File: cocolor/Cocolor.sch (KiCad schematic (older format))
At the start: 17 parts, among them P1 CONN_01X05, P2 CONN_01X05, U1 TCS3472, U2 LTC4316

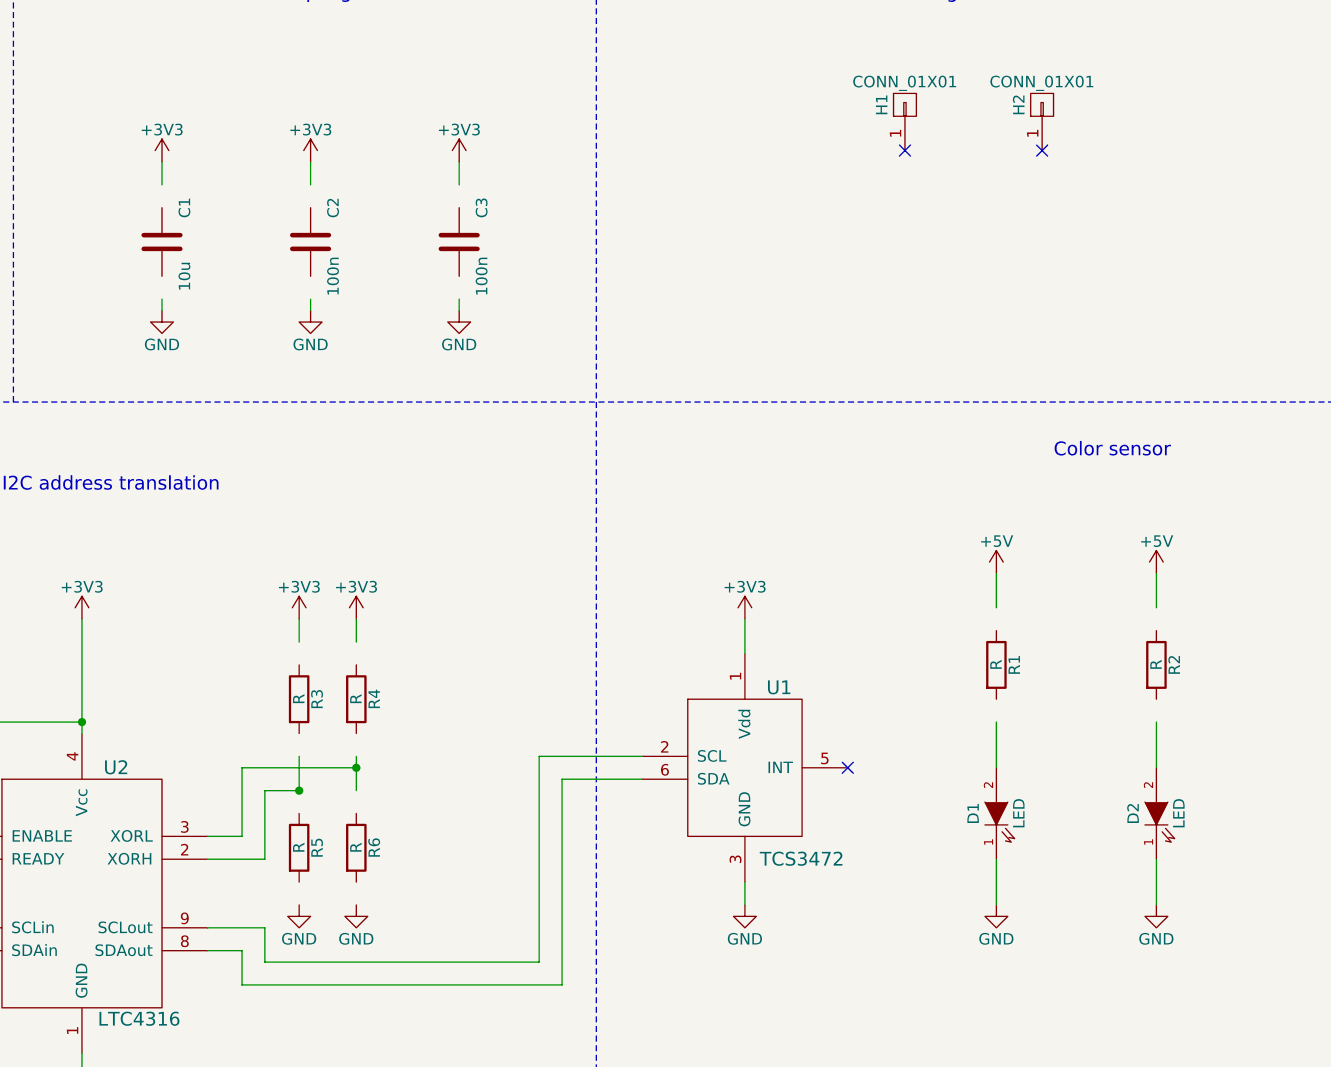
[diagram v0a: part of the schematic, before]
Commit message: fix schematic of cocolor board
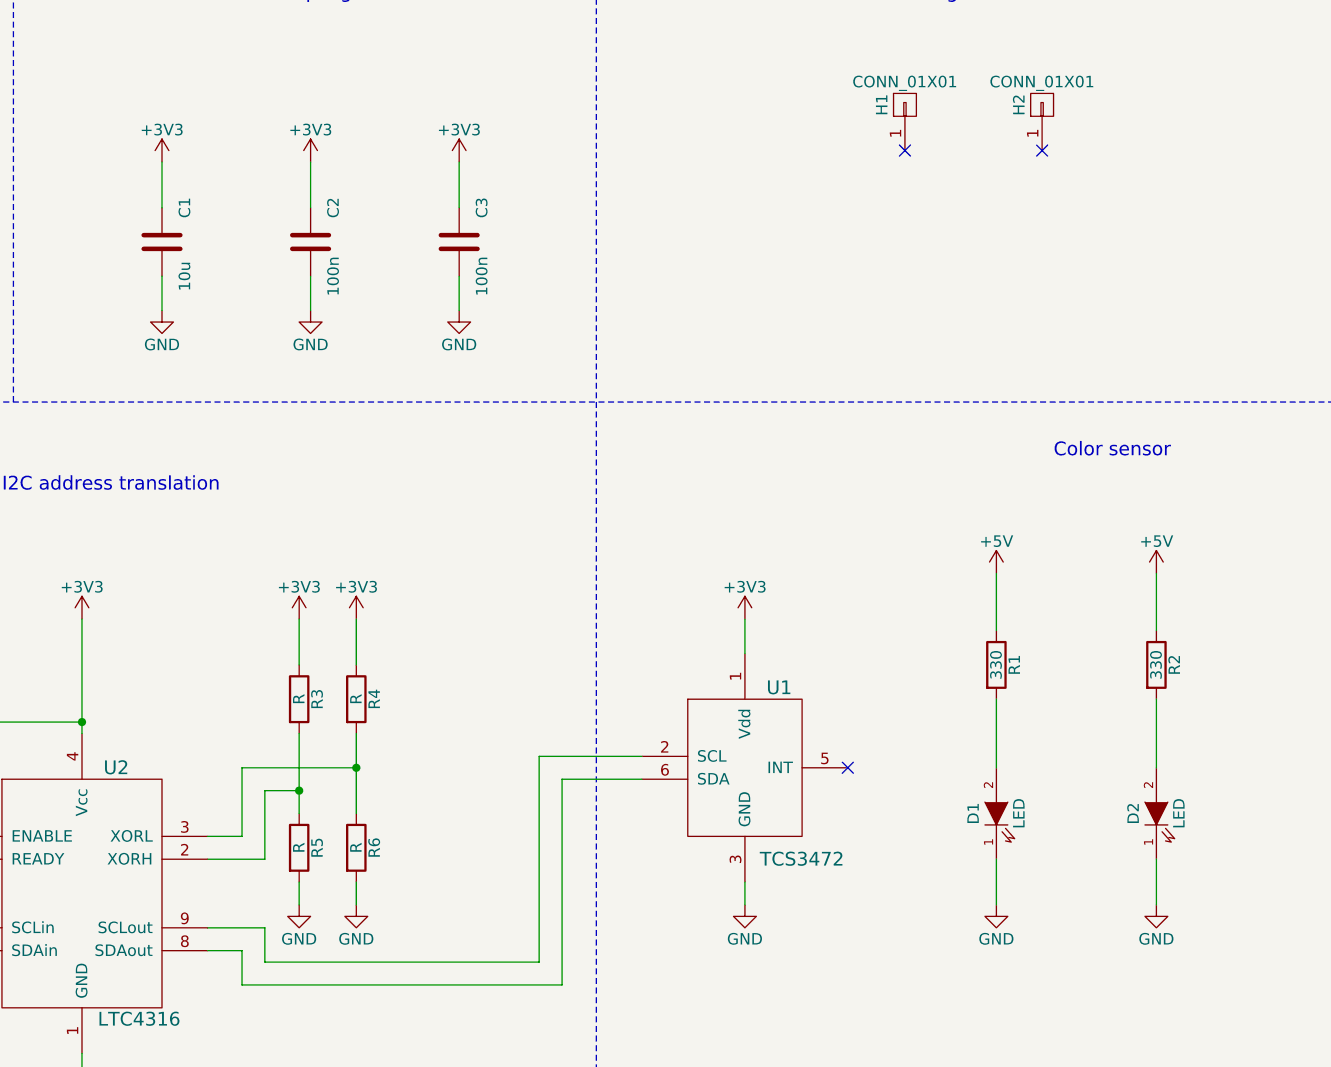
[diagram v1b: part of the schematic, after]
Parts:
- R1, R2: value R -> 330
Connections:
- wire segments 57 -> 59
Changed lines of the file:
@@
 LIBS:regul
 LIBS:references
-LIBS:pspice
 LIBS:powerint
 LIBS:power
@@
 	3400 2600 3400 500
 $Comp
-L C C1
-U 1 1 573CB74D
-P 4050 1900
-F 0 "C1" V 4150 2050 50  0000 C CNN
-F 1 "10u" V 4150 1750 50  0000 C CNN
-F 2 "" H 4050 1900 50  0000 C CNN
-F 3 "" H 4050 1900 50  0000 C CNN
-	1    4050 1900
-	1    0    0    -1
-$EndComp
-$Comp
 L GND #PWR05
 U 1 1 573CB77A
@@
 $EndComp
 $Comp
-L C C2
-U 1 1 573CB7A2
-P 4700 1900
-F 0 "C2" V 4800 2050 50  0000 C CNN
-F 1 "100n" V 4800 1750 50  0000 C CNN
-F 2 "" H 4700 1900 50  0000 C CNN
-F 3 "" H 4700 1900 50  0000 C CNN
-	1    4700 1900
-	1    0    0    -1
-$EndComp
-$Comp
 L GND #PWR07
 U 1 1 573CB7D4
@@
 $EndComp
 Wire Wire Line
-	4050 1550 4050 1650
-Wire Wire Line
-	4050 2150 4050 2200
-Wire Wire Line
-	4700 1550 4700 1650
-Wire Wire Line
-	4700 2150 4700 2200
+	4050 1550 4050 1750
+Wire Wire Line
+	4050 2050 4050 2200
+Wire Wire Line
+	4700 1550 4700 1750
+Wire Wire Line
+	4700 2050 4700 2200
 Text Notes 4150 850  0    60   ~ 0
 Power decoupling
@@
 	4400 4200 4900 4200
 Wire Wire Line
-	4900 4150 4900 4300
-Wire Wire Line
-	4650 4300 4650 4150
+	4900 4050 4900 4400
+Wire Wire Line
+	4650 4050 4650 4400
 Connection ~ 4900 4200
 Connection ~ 4650 4300
@@
 $EndComp
 Wire Wire Line
-	4900 3550 4900 3650
-Wire Wire Line
-	4650 3650 4650 3550
+	4900 3550 4900 3750
+Wire Wire Line
+	4650 3550 4650 3750
 $Comp
 L GND #PWR015
@@
 $EndComp
 $Comp
-L C C3
-U 1 1 573CD222
-P 5350 1900
-F 0 "C3" V 5450 2050 50  0000 C CNN
-F 1 "100n" V 5450 1750 50  0000 C CNN
-F 2 "" H 5350 1900 50  0000 C CNN
-F 3 "" H 5350 1900 50  0000 C CNN
-	1    5350 1900
-	1    0    0    -1
-$EndComp
-$Comp
 L +3V3 #PWR016
 U 1 1 573CD3DF
@@
 $EndComp
 Wire Wire Line
-	5350 1550 5350 1650
-Wire Wire Line
-	5350 2200 5350 2150
+	5350 1550 5350 1750
+Wire Wire Line
+	5350 2050 5350 2200
 $Comp
 L TCS3472 U1
@@
 P 8400 3750
 F 0 "R2" V 8480 3750 50  0000 C CNN
-F 1 "R" V 8400 3750 50  0000 C CNN
+F 1 "330" V 8400 3750 50  0000 C CNN
 F 2 "" H 8400 3750 50  0000 C CNN
 F 3 "" H 8400 3750 50  0000 C CNN
@@
 $EndComp
 Wire Wire Line
-	8400 4200 8400 4000
-Wire Wire Line
-	8400 3500 8400 3350
+	8400 3900 8400 4200
+Wire Wire Line
+	8400 3350 8400 3600
 $Comp
 L LED D1
@@
 P 7700 3750
 F 0 "R1" V 7780 3750 50  0000 C CNN
-F 1 "R" V 7700 3750 50  0000 C CNN
+F 1 "330" V 7700 3750 50  0000 C CNN
 F 2 "" H 7700 3750 50  0000 C CNN
 F 3 "" H 7700 3750 50  0000 C CNN
@@
 $EndComp
 Wire Wire Line
-	7700 4200 7700 4000
-Wire Wire Line
-	7700 3500 7700 3350
+	7700 3900 7700 4200
+Wire Wire Line
+	7700 3350 7700 3600
 $Comp
 L CONN_01X01 H1
@@
 NoConn ~ 7300 1500
 NoConn ~ 7900 1500
+$Comp
+L C C3
+U 1 1 573CD222
+P 5350 1900
+F 0 "C3" V 5450 2050 50  0000 C CNN
+F 1 "100n" V 5450 1750 50  0000 C CNN
+F 2 "" H 5350 1900 50  0000 C CNN
+F 3 "" H 5350 1900 50  0000 C CNN
+	1    5350 1900
+	1    0    0    -1
+$EndComp
+$Comp
+L C C2
+U 1 1 573CB7A2
+P 4700 1900
+F 0 "C2" V 4800 2050 50  0000 C CNN
+F 1 "100n" V 4800 1750 50  0000 C CNN
+F 2 "" H 4700 1900 50  0000 C CNN
+F 3 "" H 4700 1900 50  0000 C CNN
+	1    4700 1900
+	1    0    0    -1
+$EndComp
+$Comp
+L C C1
+U 1 1 573CB74D
+P 4050 1900
+F 0 "C1" V 4150 2050 50  0000 C CNN
+F 1 "10u" V 4150 1750 50  0000 C CNN
+F 2 "" H 4050 1900 50  0000 C CNN
+F 3 "" H 4050 1900 50  0000 C CNN
+	1    4050 1900
+	1    0    0    -1
+$EndComp
+Wire Wire Line
+	4650 4700 4650 4800
+Wire Wire Line
+	4900 4800 4900 4700
 $EndSCHEMATC

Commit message: cocolor layout
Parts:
- C1: footprint (none) -> espitall:C_0805_HandSoldering
- C2, C3: footprint (none) -> espitall:C_0603_HandSoldering
- D1, D2: footprint (none) -> espitall:LED_1206
- H1, H2: footprint (none) -> Mounting_Holes:MountingHole_3.2mm_M3
- P1, P2: footprint (none) -> espitall:Socket_MOLEX-KK-RM2-54mm_Lock_5pin_straight
- R1, R2, R3, R4, R5, R6: footprint (none) -> espitall:R_0603_HandSoldering
- U1: footprint (none) -> espitall:DFN-6
- U2: footprint (none) -> espitall:MSOP-10
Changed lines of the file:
@@
-EESchema Schematic File Version 2
-LIBS:xilinx
-LIBS:video
-LIBS:valves
-LIBS:ttl_ieee
-LIBS:transistors
-LIBS:transf
-LIBS:texas
-LIBS:switches
-LIBS:supertex
-LIBS:stm8
-LIBS:stm32
-LIBS:siliconi
-LIBS:silabs
-LIBS:sensors
-LIBS:rfcom
-LIBS:relays
-LIBS:regul
-LIBS:references
-LIBS:powerint
-LIBS:power
-LIBS:philips
-LIBS:opto
-LIBS:onsemi
-LIBS:nxp_armmcu
-LIBS:nordicsemi
-LIBS:msp430
-LIBS:motorola
-LIBS:motor_drivers
-LIBS:microcontrollers
-LIBS:microchip_pic32mcu
-LIBS:microchip_pic18mcu
-LIBS:microchip_pic16mcu
-LIBS:microchip_pic12mcu
-LIBS:microchip_pic10mcu
-LIBS:microchip_dspic33dsc
-LIBS:microchip
-LIBS:memory
-LIBS:maxim
-LIBS:logo
-LIBS:linear
-LIBS:ir
-LIBS:interface
-LIBS:intel
-LIBS:hc11
-LIBS:graphic
-LIBS:gennum
-LIBS:ftdi
-LIBS:elec-unifil
-LIBS:dsp
-LIBS:display
-LIBS:diode
-LIBS:digital-audio
-LIBS:device
-LIBS:dc-dc
-LIBS:cypress
-LIBS:contrib
-LIBS:conn
-LIBS:cmos_ieee
-LIBS:cmos4000
-LIBS:brooktre
-LIBS:audio
-LIBS:atmel
-LIBS:analog_switches
-LIBS:analog_devices
-LIBS:adc-dac
-LIBS:actel
-LIBS:ac-dc
-LIBS:Zilog
-LIBS:Xicor
-LIBS:Power_Management
-LIBS:Oscillators
-LIBS:Lattice
-LIBS:ESD_Protection
-LIBS:Altera
-LIBS:74xx
-LIBS:74xgxx
-LIBS:Symbols_Transformer-Diskrete_RevA
-LIBS:Symbols_Socket-DIN41612_RevA
-LIBS:Symbols_Microcontroller_Philips-NXP_RevA_06Oct2013
-LIBS:Symbols_ICs-Opto_RevB_16Sep2013
-LIBS:Symbols_ICs-Diskrete_RevD10
-LIBS:Symbols_EN60617_13Mar2013
-LIBS:Symbols_EN60617-10_HF-Radio_DRAFT_12Sep2013
-LIBS:Symbols_DCDC-ACDC-Converter_RevC_20Jul2012
-LIBS:SymbolsSimilarEN60617+oldDIN617-RevE8
+EESchema Schematic File Version 3
 LIBS:espitall
 LIBS:Cocolor-cache
-EELAYER 25 0
+EELAYER 26 0
 EELAYER END
 $Descr A4 11693 8268
@@
 	2100 5000 2100 1900
 Connection ~ 2100 1900
-$Comp
-L LTC4316 U2
-U 1 1 573CCB68
-P 3700 4750
-F 0 "U2" H 3850 5300 60  0000 C CNN
-F 1 "LTC4316" H 3950 4200 60  0000 C CNN
-F 2 "" H 3700 4750 60  0000 C CNN
-F 3 "" H 3700 4750 60  0000 C CNN
-	1    3700 4750
-	1    0    0    -1
-$EndComp
 Wire Wire Line
 	3150 4500 3050 4500
@@
 F 0 "R3" V 4730 3900 50  0000 C CNN
 F 1 "R" V 4650 3900 50  0000 C CNN
-F 2 "" H 4650 3900 50  0000 C CNN
+F 2 "espitall:R_0603_HandSoldering" H 4650 3900 50  0001 C CNN
 F 3 "" H 4650 3900 50  0000 C CNN
 	1    4650 3900
-	1    0    0    -1
-$EndComp
-$Comp
-L R R5
-U 1 1 573CCC89
-P 4650 4550
-F 0 "R5" V 4730 4550 50  0000 C CNN
-F 1 "R" V 4650 4550 50  0000 C CNN
-F 2 "" H 4650 4550 50  0000 C CNN
-F 3 "" H 4650 4550 50  0000 C CNN
-	1    4650 4550
-	1    0    0    -1
-$EndComp
-$Comp
-L R R6
-U 1 1 573CCCC4
-P 4900 4550
-F 0 "R6" V 4980 4550 50  0000 C CNN
-F 1 "R" V 4900 4550 50  0000 C CNN
-F 2 "" H 4900 4550 50  0000 C CNN
-F 3 "" H 4900 4550 50  0000 C CNN
-	1    4900 4550
-	1    0    0    -1
-$EndComp
-$Comp
-L R R4
-U 1 1 573CCCF6
-P 4900 3900
-F 0 "R4" V 4980 3900 50  0000 C CNN
-F 1 "R" V 4900 3900 50  0000 C CNN
-F 2 "" H 4900 3900 50  0000 C CNN
-F 3 "" H 4900 3900 50  0000 C CNN
-	1    4900 3900
 	1    0    0    -1
 $EndComp
@@
 	5350 2050 5350 2200
 $Comp
-L TCS3472 U1
-U 1 1 573CD6D5
-P 6600 4200
-F 0 "U1" H 6750 4550 60  0000 C CNN
-F 1 "TCS3472" H 6850 3800 60  0000 C CNN
-F 2 "" H 6600 4200 60  0000 C CNN
-F 3 "" H 6600 4200 60  0000 C CNN
-	1    6600 4200
-	1    0    0    -1
-$EndComp
-$Comp
 L +3V3 #PWR017
 U 1 1 573CD7A4
@@
 F 0 "P1" H 1250 2200 50  0000 C CNN
 F 1 "CONN_01X05" V 1350 1900 50  0000 C CNN
-F 2 "" H 1250 1900 50  0000 C CNN
+F 2 "espitall:Socket_MOLEX-KK-RM2-54mm_Lock_5pin_straight" H 1250 1900 50  0001 C CNN
 F 3 "" H 1250 1900 50  0000 C CNN
 	1    1250 1900
@@
 F 0 "P2" H 2750 2200 50  0000 C CNN
 F 1 "CONN_01X05" V 2850 1900 50  0000 C CNN
-F 2 "" H 2750 1900 50  0000 C CNN
+F 2 "espitall:Socket_MOLEX-KK-RM2-54mm_Lock_5pin_straight" H 2750 1900 50  0001 C CNN
 F 3 "" H 2750 1900 50  0000 C CNN
 	1    2750 1900
@@
 Wire Wire Line
 	2500 1700 2550 1700
-$Comp
-L LED D2
-U 1 1 573CE5E1
-P 8400 4400
-F 0 "D2" H 8400 4500 50  0000 C CNN
-F 1 "LED" H 8400 4300 50  0000 C CNN
-F 2 "" H 8400 4400 50  0000 C CNN
-F 3 "" H 8400 4400 50  0000 C CNN
-	1    8400 4400
-	0    -1   -1   0
-$EndComp
 $Comp
 L GND #PWR021
@@
 	1    0    0    -1
 $EndComp
-$Comp
-L R R2
-U 1 1 573CE7BD
-P 8400 3750
-F 0 "R2" V 8480 3750 50  0000 C CNN
-F 1 "330" V 8400 3750 50  0000 C CNN
-F 2 "" H 8400 3750 50  0000 C CNN
-F 3 "" H 8400 3750 50  0000 C CNN
-	1    8400 3750
-	1    0    0    -1
-$EndComp
 Wire Wire Line
 	8400 3900 8400 4200
@@
 F 0 "D1" H 7700 4500 50  0000 C CNN
 F 1 "LED" H 7700 4300 50  0000 C CNN
-F 2 "" H 7700 4400 50  0000 C CNN
+F 2 "espitall:LED_1206" H 7700 4400 50  0001 C CNN
 F 3 "" H 7700 4400 50  0000 C CNN
 	1    7700 4400
@@
 F 0 "R1" V 7780 3750 50  0000 C CNN
 F 1 "330" V 7700 3750 50  0000 C CNN
-F 2 "" H 7700 3750 50  0000 C CNN
+F 2 "espitall:R_0603_HandSoldering" H 7700 3750 50  0001 C CNN
 F 3 "" H 7700 3750 50  0000 C CNN
 	1    7700 3750
@@
 F 0 "H1" H 7300 1400 50  0000 C CNN
 F 1 "CONN_01X01" V 7400 1300 50  0000 C CNN
-F 2 "" H 7300 1300 50  0000 C CNN
+F 2 "Mounting_Holes:MountingHole_3.2mm_M3" H 7300 1300 50  0001 C CNN
 F 3 "" H 7300 1300 50  0000 C CNN
 	1    7300 1300
@@
 F 0 "H2" H 7900 1400 50  0000 C CNN
 F 1 "CONN_01X01" V 8000 1300 50  0000 C CNN
-F 2 "" H 7900 1300 50  0000 C CNN
+F 2 "Mounting_Holes:MountingHole_3.2mm_M3" H 7900 1300 50  0001 C CNN
 F 3 "" H 7900 1300 50  0000 C CNN
 	1    7900 1300
@@
 NoConn ~ 7900 1500
 $Comp
-L C C3
-U 1 1 573CD222
-P 5350 1900
-F 0 "C3" V 5450 2050 50  0000 C CNN
-F 1 "100n" V 5450 1750 50  0000 C CNN
-F 2 "" H 5350 1900 50  0000 C CNN
-F 3 "" H 5350 1900 50  0000 C CNN
-	1    5350 1900
-	1    0    0    -1
-$EndComp
-$Comp
 L C C2
 U 1 1 573CB7A2
@@
 F 0 "C2" V 4800 2050 50  0000 C CNN
 F 1 "100n" V 4800 1750 50  0000 C CNN
-F 2 "" H 4700 1900 50  0000 C CNN
+F 2 "espitall:C_0603_HandSoldering" H 4700 1900 50  0001 C CNN
 F 3 "" H 4700 1900 50  0000 C CNN
 	1    4700 1900
@@
 F 0 "C1" V 4150 2050 50  0000 C CNN
 F 1 "10u" V 4150 1750 50  0000 C CNN
-F 2 "" H 4050 1900 50  0000 C CNN
+F 2 "espitall:C_0805_HandSoldering" H 4050 1900 50  0001 C CNN
 F 3 "" H 4050 1900 50  0000 C CNN
 	1    4050 1900
@@
 Wire Wire Line
 	4900 4800 4900 4700
+$Comp
+L C C3
+U 1 1 57893CF6
+P 5350 1900
+F 0 "C3" V 5450 2050 50  0000 C CNN
+F 1 "100n" V 5450 1750 50  0000 C CNN
+F 2 "espitall:C_0603_HandSoldering" H 5350 1900 50  0001 C CNN
+F 3 "" H 5350 1900 50  0000 C CNN
+	1    5350 1900
+	1    0    0    -1
+$EndComp
+$Comp
+L R R4
+U 1 1 57893FB8
+P 4900 3900
+F 0 "R4" V 4980 3900 50  0000 C CNN
+F 1 "R" V 4900 3900 50  0000 C CNN
+F 2 "espitall:R_0603_HandSoldering" H 4900 3900 50  0001 C CNN
+F 3 "" H 4900 3900 50  0000 C CNN
+	1    4900 3900
+	1    0    0    -1
+$EndComp
+$Comp
+L R R6
+U 1 1 57893FFD
+P 4900 4550
+F 0 "R6" V 4980 4550 50  0000 C CNN
+F 1 "R" V 4900 4550 50  0000 C CNN
+F 2 "espitall:R_0603_HandSoldering" H 4900 4550 50  0001 C CNN
+F 3 "" H 4900 4550 50  0000 C CNN
+	1    4900 4550
+	1    0    0    -1
+$EndComp
+$Comp
+L R R5
+U 1 1 57894047
+P 4650 4550
+F 0 "R5" V 4730 4550 50  0000 C CNN
+F 1 "R" V 4650 4550 50  0000 C CNN
+F 2 "espitall:R_0603_HandSoldering" H 4650 4550 50  0001 C CNN
+F 3 "" H 4650 4550 50  0000 C CNN
+	1    4650 4550
+	1    0    0    -1
+$EndComp
+$Comp
+L R R2
+U 1 1 578942A4
+P 8400 3750
+F 0 "R2" V 8480 3750 50  0000 C CNN
+F 1 "330" V 8400 3750 50  0000 C CNN
+F 2 "espitall:R_0603_HandSoldering" H 8400 3750 50  0001 C CNN
+F 3 "" H 8400 3750 50  0000 C CNN
+	1    8400 3750
+	1    0    0    -1
+$EndComp
+$Comp
+L LED D2
+U 1 1 57894509
+P 8400 4400
+F 0 "D2" H 8400 4500 50  0000 C CNN
+F 1 "LED" H 8400 4300 50  0000 C CNN
+F 2 "espitall:LED_1206" H 8400 4400 50  0001 C CNN
+F 3 "" H 8400 4400 50  0000 C CNN
+	1    8400 4400
+	0    -1   -1   0
+$EndComp
+$Comp
+L LTC4316 U2
+U 1 1 59EC9CAF
+P 3700 4750
+F 0 "U2" H 3700 5650 60  0000 C CNN
+F 1 "LTC4316" H 3700 5544 60  0000 C CNN
+F 2 "espitall:MSOP-10" H 3750 5200 60  0001 C CNN
+F 3 "" H 3700 4750 60  0000 C CNN
+	1    3700 4750
+	1    0    0    -1
+$EndComp
+$Comp
+L TCS3472 U1
+U 1 1 59ECA076
+P 6600 4200
+F 0 "U1" H 7091 4253 60  0000 L CNN
+F 1 "TCS3472" H 7091 4147 60  0000 L CNN
+F 2 "espitall:DFN-6" H 6650 4450 60  0001 C CNN
+F 3 "" H 6600 4200 60  0000 C CNN
+	1    6600 4200
+	1    0    0    -1
+$EndComp
 $EndSCHEMATC

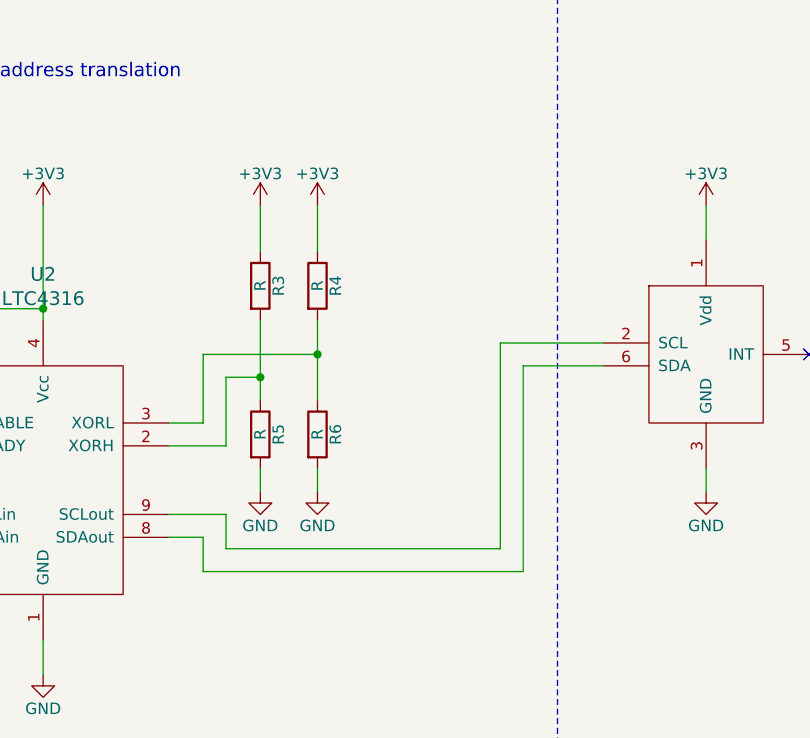
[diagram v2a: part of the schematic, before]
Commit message: Add 3D file for Cocolor sensor
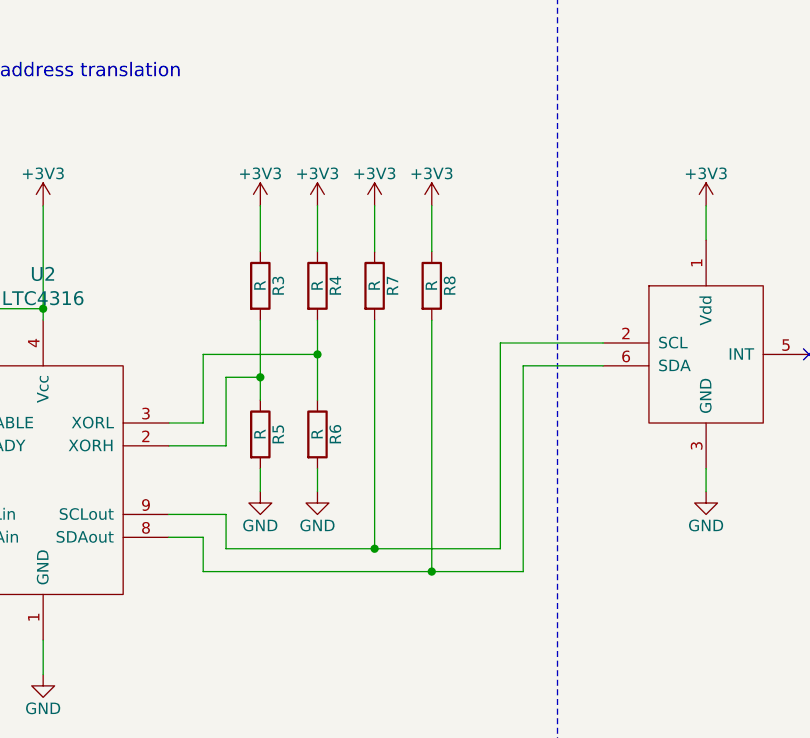
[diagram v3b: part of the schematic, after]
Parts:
- added R7, R8: R, espitall:R_0603_HandSoldering, symbol R
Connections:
- net +3V3: now also R7.1, R8.1
- net at U1.6 (SDA), U2.8 (SDAout): now also R8.2
- net at U1.2 (SCL), U2.9 (SCLout): now also R7.2
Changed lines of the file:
@@
 	1    0    0    -1
 $EndComp
+$Comp
+L R R7
+U 1 1 59F16651
+P 5150 3900
+F 0 "R7" V 5230 3900 50  0000 C CNN
+F 1 "R" V 5150 3900 50  0000 C CNN
+F 2 "espitall:R_0603_HandSoldering" H 5150 3900 50  0001 C CNN
+F 3 "" H 5150 3900 50  0000 C CNN
+	1    5150 3900
+	1    0    0    -1
+$EndComp
+$Comp
+L +3V3 #PWR025
+U 1 1 59F1668F
+P 5150 3550
+F 0 "#PWR025" H 5150 3400 50  0001 C CNN
+F 1 "+3V3" H 5150 3690 50  0000 C CNN
+F 2 "" H 5150 3550 50  0000 C CNN
+F 3 "" H 5150 3550 50  0000 C CNN
+	1    5150 3550
+	1    0    0    -1
+$EndComp
+$Comp
+L +3V3 #PWR026
+U 1 1 59F166BE
+P 5400 3550
+F 0 "#PWR026" H 5400 3400 50  0001 C CNN
+F 1 "+3V3" H 5400 3690 50  0000 C CNN
+F 2 "" H 5400 3550 50  0000 C CNN
+F 3 "" H 5400 3550 50  0000 C CNN
+	1    5400 3550
+	1    0    0    -1
+$EndComp
+$Comp
+L R R8
+U 1 1 59F1672D
+P 5400 3900
+F 0 "R8" V 5480 3900 50  0000 C CNN
+F 1 "R" V 5400 3900 50  0000 C CNN
+F 2 "espitall:R_0603_HandSoldering" H 5400 3900 50  0001 C CNN
+F 3 "" H 5400 3900 50  0000 C CNN
+	1    5400 3900
+	1    0    0    -1
+$EndComp
+Wire Wire Line
+	5400 3750 5400 3550
+Wire Wire Line
+	5150 3550 5150 3750
+Wire Wire Line
+	5150 4050 5150 5050
+Connection ~ 5150 5050
+Wire Wire Line
+	5400 4050 5400 5150
+Connection ~ 5400 5150
 $EndSCHEMATC
